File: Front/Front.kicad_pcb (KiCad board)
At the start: 2 copper layers, 40 x 40 mm, 42 parts, among them J1 USB_B_Micro, Q1 BC849, Q2 BC849, SW2 SW_Push, U1 CH340C, U10 ESP32-WROOM-32, U2 CJVL53L0XV2, U3 SPX3819M5-L-3-3

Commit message: V0.2: Redo front schematic and PCB
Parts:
- removed D1: BLUE, LED_SMD:LED_0805_2012Metric_Pad1.15x1.40mm_HandSolder
- removed D2: GREEN, LED_SMD:LED_0805_2012Metric_Pad1.15x1.40mm_HandSolder
- removed G***: LOGO, Print:d1
- removed H17: VBS, Custom:Mounting_Pad_Power
- removed SW2: SW_Push, Button_Switch_SMD:Panasonic_EVQPUJ_EVQPUA
- added H25: LED1, Custom:Mounting_Pad_Signal, F.Cu at (205.7, 105.0)
- added H26: LED2, Custom:Mounting_Pad_Signal, F.Cu at (208.3, 105.0)
- added H27: TCH2, Custom:Mounting_Pad_Touch, F.Cu at (210.8, 104.2)
- added H28: TCH1, Custom:Mounting_Pad_Touch, F.Cu at (220.2, 104.2)
- added SW1: SW_DPDT_x2, Custom:JS102011SAQN, F.Cu at (230.7, 112.7)
- H1: value VBUS -> PWR
- H16: value ORST -> O~RST
- R3, R4: value 150 -> 510
- moved R18 27.6 mm to (204.4, 122.8)
- moved U3 27.5 mm to (227.2, 112.7), turned to 90 degrees
- moved R4 26.8 mm to (204.4, 129.9), turned to 90 degrees
- moved R3 24.7 mm to (204.4, 126.3), turned to 90 degrees
- moved Q1 6.78 mm to (197.3, 133.7), turned to 180 degrees
- moved Q2 6.68 mm to (203.9, 133.7), turned to 0 degrees
- moved R2 3.85 mm to (200.7, 132.2), turned to 180 degrees
- moved H1 3.50 mm to (200.2, 105.5)
- moved H11 3.50 mm to (203.2, 105.0)
- moved U1 3.11 mm to (199.4, 124.5)
- moved C1 2.28 mm to (199.4, 118.3), turned to 0 degrees
- moved R1 1.15 mm to (200.7, 135.2), turned to 180 degrees
- moved C2 0.97 mm to (204.4, 119.2)
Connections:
- R3 pad 1: Net-(D1-Pad2) -> /TOUCH1
- R3 pad 2: /STATUS_LED_BLUE -> Net-(H28-Pad1)
- R4 pad 2: /STATUS_LED_GRN -> /TOUCH2
- U10 pad 10: (no net) -> /LED1
- U10 pad 11: (no net) -> /LED2
- U10 pad 12: /ED_IN1 -> /M1_AOUT2
- U10 pad 13: (no net) -> /M1_BOUT1
- U10 pad 14: (no net) -> /M1_BOUT2
- U10 pad 16: /M1_BOUT2 -> /M1_AOUT1
- U10 pad 17: /M1_BOUT1 -> (no net)
- U10 pad 18: /M1_AOUT2 -> (no net)
- U10 pad 19: /M1_AOUT1 -> (no net)
- U10 pad 20: /M2_AOUT1 -> (no net)
- U10 pad 21: /M2_AOUT2 -> (no net)
- U10 pad 22: /M2_BOUT1 -> (no net)
- U10 pad 23: /M2_BOUT2 -> /M2_AOUT1
- U10 pad 24: /M1_M2_~SLEEP -> /M2_AOUT2
- U10 pad 26: (no net) -> /M2_BOUT1
- U10 pad 27: /ED_IN2 -> /M2_BOUT2
- U10 pad 28: /OD_SCL -> /M1_M2_~SLEEP
- U10 pad 29: /OD_SDA -> /OD_SCL
- U10 pad 30: /OD_SHUT -> /OD_SDA
- U10 pad 31: /OD_INTERRUPT -> /OD_SHUT
- U10 pad 4: (no net) -> /ED_IN1
- U10 pad 5: (no net) -> /ED_IN2
- U10 pad 7: /STATUS_LED_GRN -> /OD_INTERRUPT
- U10 pad 8: /STATUS_LED_BLUE -> /TOUCH1
- U10 pad 9: (no net) -> /TOUCH2
- U3 pad 1: VBUS -> Net-(SW1-Pad2)
- U3 pad 3: VBUS -> Net-(SW1-Pad2)
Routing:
- net Net-(H28-Pad1): track 0.00 -> 43.8 mm, vias 0 -> 2
- net Net-(H27-Pad1): track 2.14 -> 38.5 mm, vias 0 -> 2
- net /STATUS_LED_BLUE: track 35.8 -> 0.00 mm
- net /LED2: track 0.00 -> 33.2 mm
- net /STATUS_LED_GRN: track 32.2 -> 0.00 mm
- net /LED1: track 0.00 -> 31.1 mm
- net /~RST: track 52.8 -> 27.0 mm
- net VBUS: track 21.9 -> 44.7 mm, vias 5 -> 2
- net /ED_IN2: track 11.1 -> 32.6 mm, vias 0 -> 4
- net +3V3: track 96.7 -> 111.3 mm, vias 8 -> 6
- net /ED_IN1: track 15.2 -> 26.5 mm, vias 0 -> 2
- net /GPIO0: track 30.0 -> 21.6 mm
- net /OD_INTERRUPT: track 17.7 -> 25.8 mm, vias 0 -> 2
- net Net-(SW1-Pad2): track 0.00 -> 7.93 mm
- net GND: track 27.1 -> 20.2 mm, vias 43 -> 36
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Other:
- outline, holes or cut-outs redrawn
- board text added: "Cuby V0.2"
- board text removed: "Cuby V0.1"

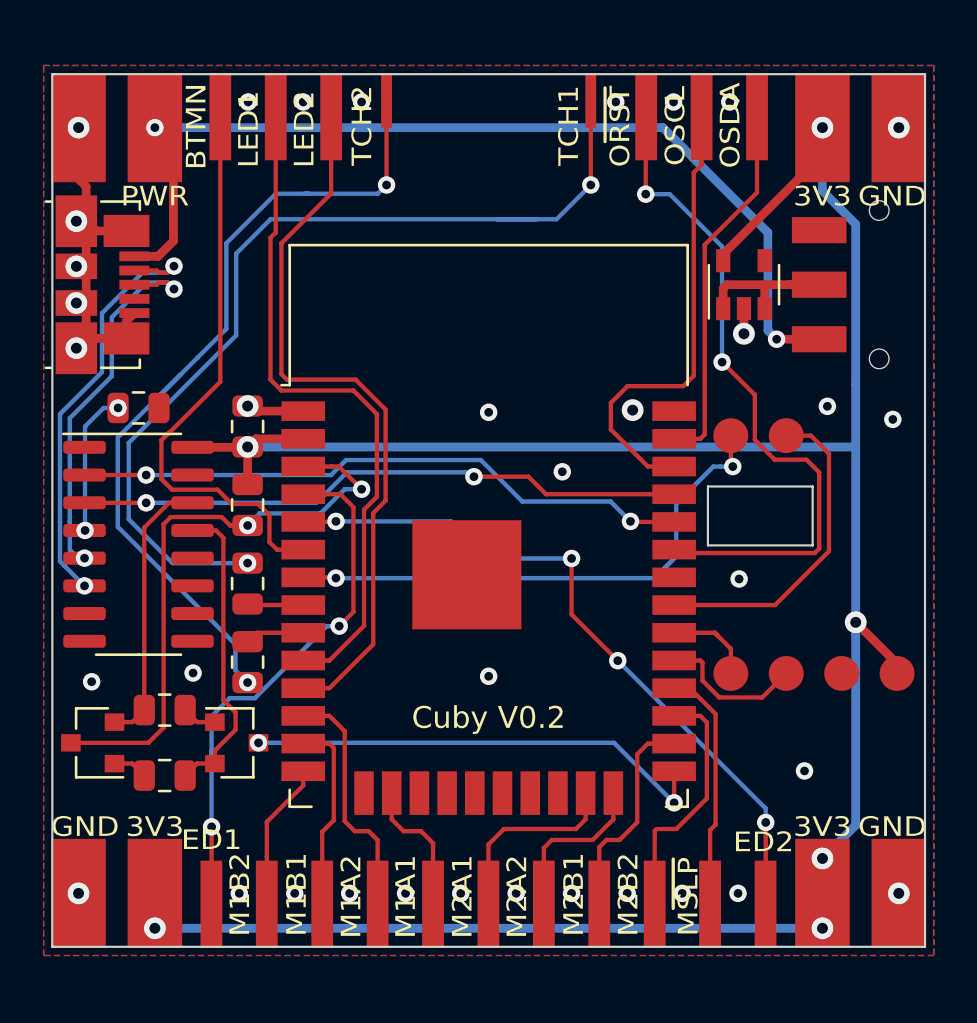
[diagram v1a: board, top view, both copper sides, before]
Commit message: updated bottom (motor placement, sharp sensor), front redesign, start op top redesign
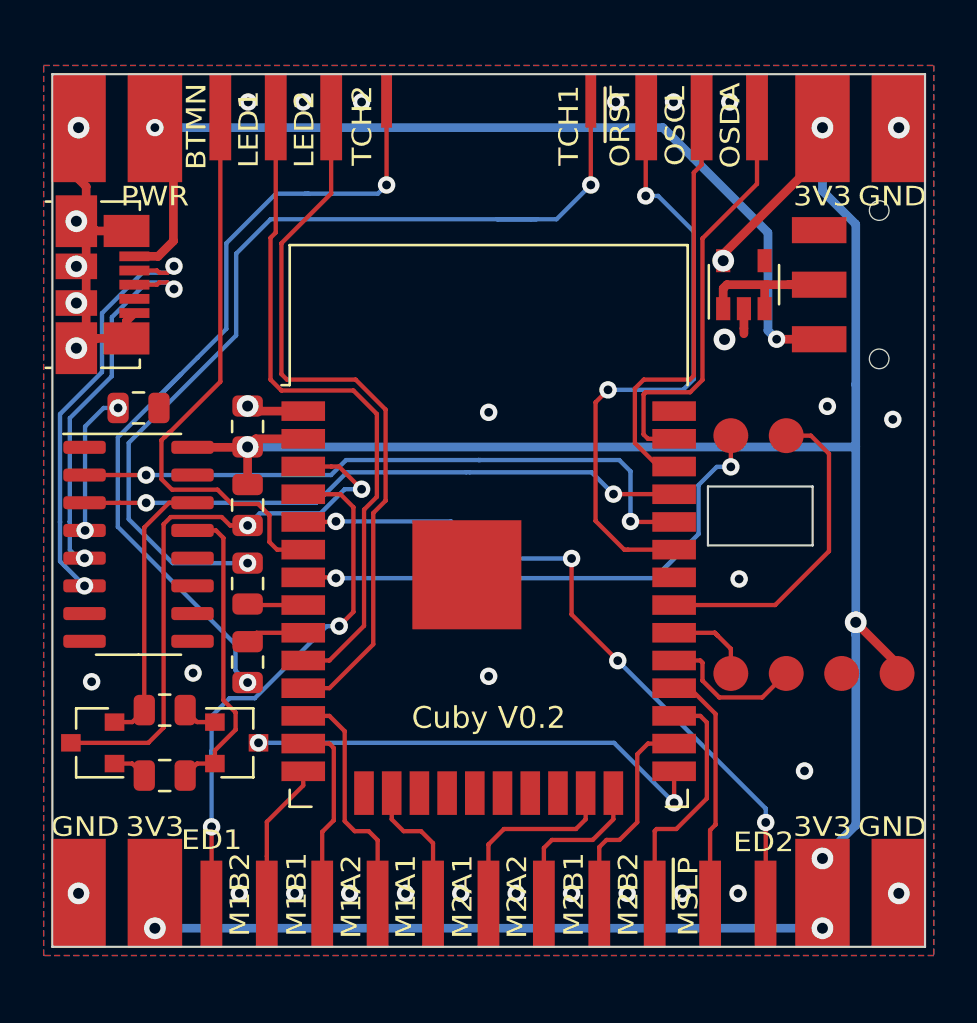
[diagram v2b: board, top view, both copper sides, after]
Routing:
- net /OLED_~RES: track 31.4 -> 27.8 mm
- net /OLED_SDA: track 17.0 -> 19.4 mm
- net /TXD-RXD: track 28.5 -> 29.9 mm
- net /OLED_SCL: track 21.2 -> 19.7 mm
- net GND: vias 36 -> 34
- net +3V3: vias 6 -> 7

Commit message: Update Top V0.2, small changes to motor placement
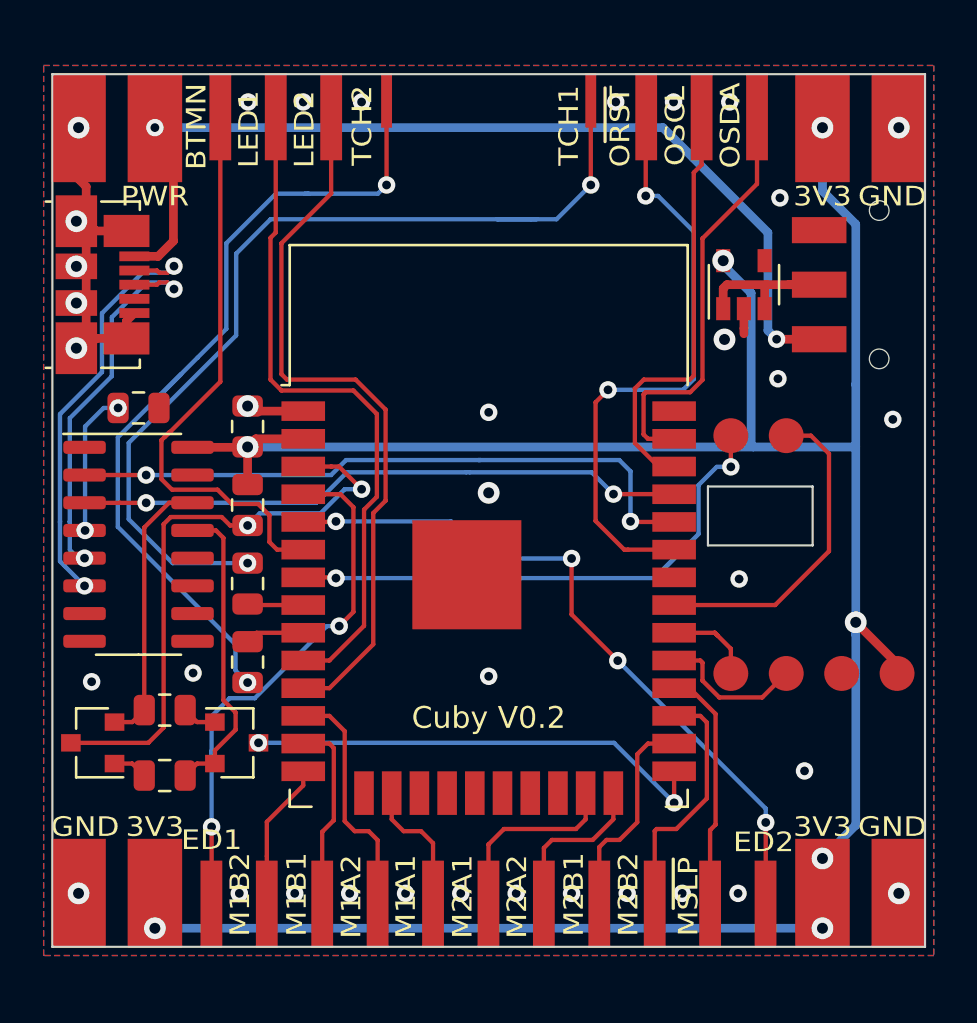
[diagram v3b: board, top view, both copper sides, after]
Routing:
- net +3V3: track 111.3 -> 113.7 mm
- net GND: vias 34 -> 36
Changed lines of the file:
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@@
     (thickness 1.6)
     (drawings 9)
-    (tracks 418)
+    (tracks 423)
     (zones 0)
     (modules 42)
@@
   (via (at 204.45 118.2125) (size 1) (drill 0.5) (layers F.Cu B.Cu) (net 1) (status 30))
   (via (at 234.025 118.825) (size 0.8) (drill 0.4) (layers F.Cu B.Cu) (net 1))
-  (via (at 231.025 118.225) (size 0.8) (drill 0.4) (layers F.Cu B.Cu) (net 1))
+  (via (at 228.76 116.96) (size 0.8) (drill 0.4) (layers F.Cu B.Cu) (net 1))
+  (via (at 228.85 108.67) (size 0.8) (drill 0.4) (layers F.Cu B.Cu) (net 1))
+  (via (at 215.5 122.19) (size 1) (drill 0.5) (layers F.Cu B.Cu) (net 1))
   (via (at 197.00001 123.915) (size 0.8) (drill 0.4) (layers F.Cu B.Cu) (net 2) (status 30))
   (via (at 198.5125 118.3) (size 0.8) (drill 0.4) (layers F.Cu B.Cu) (net 2) (status 30))
@@
   (segment (start 230.8 108.35) (end 232.325 109.875) (width 0.4) (layer B.Cu) (net 4))
   (segment (start 230.8 105.45) (end 230.8 108.35) (width 0.4) (layer B.Cu) (net 4))
-  (segment (start 226.25 111.25) (end 226.25 111.55) (width 0.4) (layer F.Cu) (net 4) (status 30))
-  (segment (start 230.8 106.7) (end 226.25 111.25) (width 0.4) (layer F.Cu) (net 4) (status 30))
   (segment (start 230.8 105.45) (end 230.8 106.7) (width 0.4) (layer F.Cu) (net 4) (status 30))
   (via (at 204.45 120.0875) (size 1) (drill 0.5) (layers F.Cu B.Cu) (net 4) (status 30))
@@
   (segment (start 232.325 120.075) (end 232.325 128.125) (width 0.4) (layer B.Cu) (net 4))
   (segment (start 232.3125 120.0875) (end 232.325 120.075) (width 0.4) (layer B.Cu) (net 4))
-  (segment (start 204.45 120.0875) (end 232.3125 120.0875) (width 0.4) (layer B.Cu) (net 4))
   (via (at 226.25 111.55) (size 1) (drill 0.5) (layers F.Cu B.Cu) (net 4))
+  (segment (start 226.25 111.755) (end 227.53 113.035) (width 0.4) (layer B.Cu) (net 4))
+  (segment (start 226.25 111.55) (end 226.25 111.755) (width 0.4) (layer B.Cu) (net 4))
+  (segment (start 227.53 119.99) (end 227.6275 120.0875) (width 0.4) (layer B.Cu) (net 4))
+  (segment (start 227.53 113.035) (end 227.53 119.99) (width 0.4) (layer B.Cu) (net 4))
+  (segment (start 204.45 120.0875) (end 227.6275 120.0875) (width 0.4) (layer B.Cu) (net 4))
+  (segment (start 227.6275 120.0875) (end 232.3125 120.0875) (width 0.4) (layer B.Cu) (net 4))
   (segment (start 203.65 123.6875) (end 203.2625 123.3) (width 0.2) (layer F.Cu) (net 5))
   (segment (start 204.45 123.6875) (end 203.65 123.6875) (width 0.2) (layer F.Cu) (net 5) (status 10))

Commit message: finish top, changes to front, added graphic
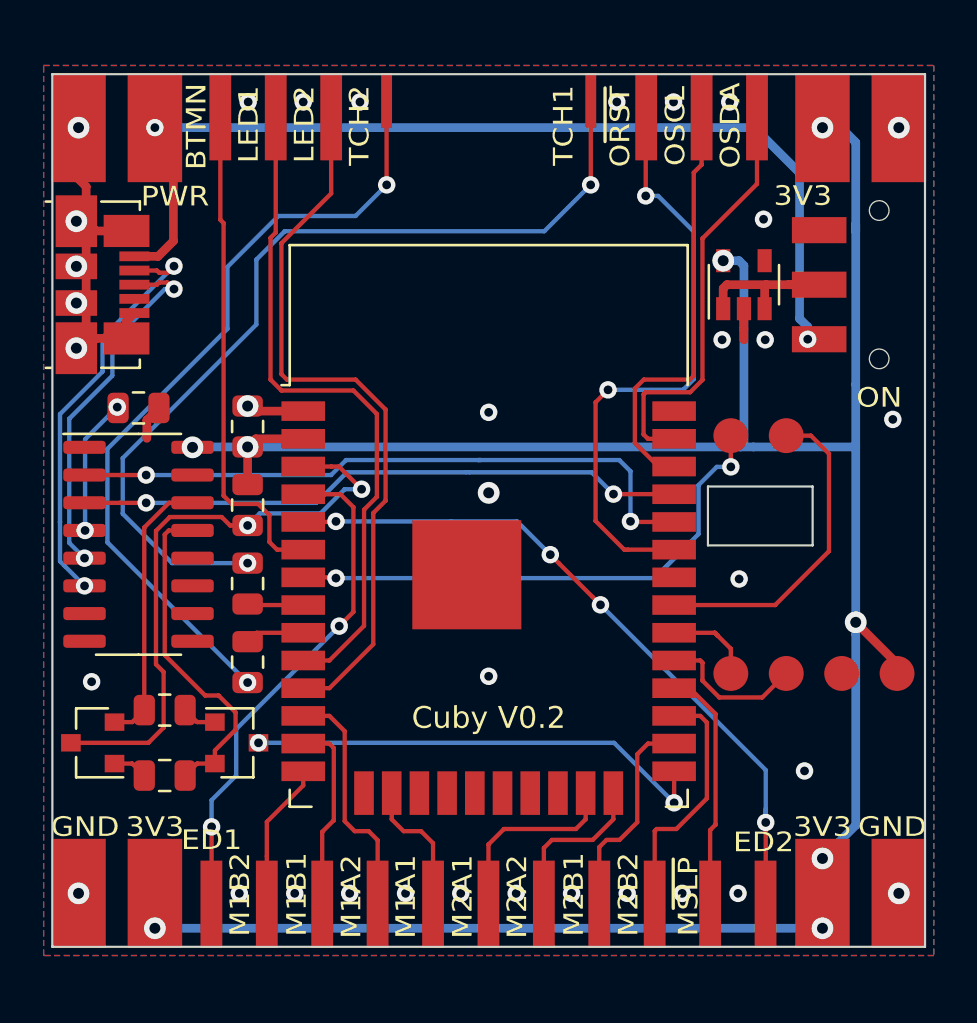
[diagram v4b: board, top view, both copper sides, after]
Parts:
- added G1: Graphic, Print:d1, B.Cu at (215.5, 123.0)
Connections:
- net Net-(H27-Pad1) renamed /T2
- net Net-(H28-Pad1) renamed /T1
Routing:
- net /BAT_MON: track 26.6 -> 22.8 mm
- net /T1: track 43.8 -> 41.5 mm
- net GND: track 20.2 -> 22.1 mm, vias 36 -> 35
- net /T2: track 38.5 -> 36.8 mm
- net /ED_IN1: track 26.5 -> 24.9 mm
- net Net-(Q2-Pad2): track 14.1 -> 15.5 mm
- net +3V3: track 113.7 -> 114.8 mm, vias 7 -> 8
- net VBUS: track 44.7 -> 45.8 mm
- net /D+: track 18.0 -> 17.1 mm
- net /D-: track 20.0 -> 19.3 mm
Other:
- net class Touch added: clearance 0.5, trace_width 0.2, via_dia 0.8, via_drill 0.4
- board text added: "ON"

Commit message: finishing touches, moved touch traces to back
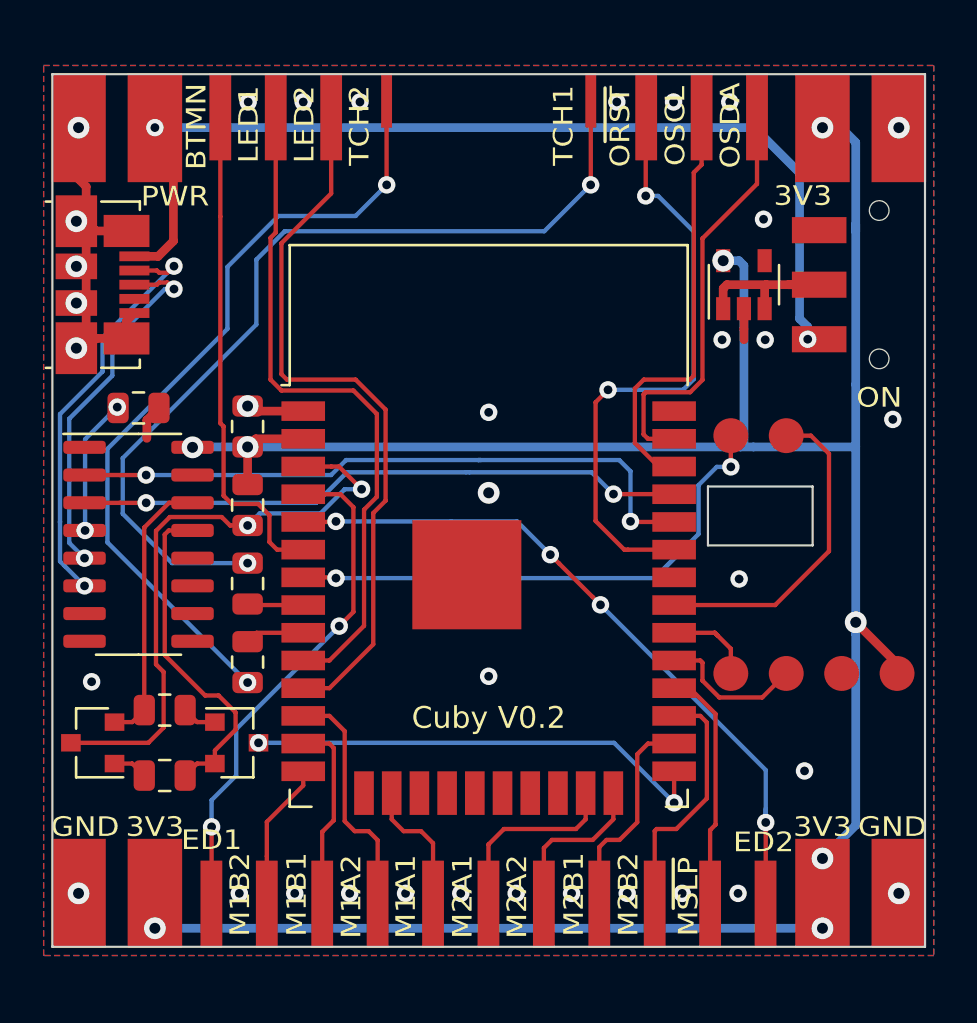
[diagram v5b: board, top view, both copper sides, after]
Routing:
- net +3V3: track 114.8 -> 113.6 mm
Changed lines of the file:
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@@
   (segment (start 204.4325 120.105) (end 204.45 120.0875) (width 0.4) (layer F.Cu) (net 4) (status 30))
   (segment (start 204.45 121.8125) (end 204.45 120.0875) (width 0.4) (layer F.Cu) (net 4) (status 30))
-  (segment (start 230.8 105.45) (end 230.8 106.7) (width 0.4) (layer F.Cu) (net 4) (status 30))
   (via (at 204.45 120.0875) (size 1) (drill 0.5) (layers F.Cu B.Cu) (net 4) (status 30))
   (segment (start 232.325 137.425) (end 230.8 138.95) (width 0.4) (layer B.Cu) (net 4))
@@
   (segment (start 207 135.605) (end 205.33 137.275) (width 0.2) (layer F.Cu) (net 14))
   (segment (start 207 134.955) (end 207 135.605) (width 0.2) (layer F.Cu) (net 14) (status 10))
+  (segment (start 203.2 109.525) (end 203.2 104.95) (width 0.2) (layer F.Cu) (net 15))
+  (segment (start 203.2 119) (end 203.2 109.525) (width 0.2) (layer F.Cu) (net 15))
+  (segment (start 203.34999 122.322906) (end 203.34999 119.14999) (width 0.2) (layer F.Cu) (net 15))
+  (segment (start 207 124.795) (end 205.8 124.795) (width 0.2) (layer F.Cu) (net 15))
   (segment (start 205.8 124.795) (end 205.45001 124.44501) (width 0.2) (layer F.Cu) (net 15))
-  (segment (start 207 124.795) (end 205.8 124.795) (width 0.2) (layer F.Cu) (net 15) (status 10))
   (segment (start 205.45001 124.44501) (end 205.45001 123.218516) (width 0.2) (layer F.Cu) (net 15))
   (segment (start 205.45001 123.218516) (end 204.931504 122.70001) (width 0.2) (layer F.Cu) (net 15))
   (segment (start 204.931504 122.70001) (end 203.727094 122.70001) (width 0.2) (layer F.Cu) (net 15))
-  (segment (start 203.34999 109.82499) (end 203.2 109.675) (width 0.2) (layer F.Cu) (net 15))
-  (segment (start 203.34999 122.322906) (end 203.34999 109.82499) (width 0.2) (layer F.Cu) (net 15))
+  (segment (start 203.34999 119.14999) (end 203.2 119) (width 0.2) (layer F.Cu) (net 15))
   (segment (start 203.727094 122.70001) (end 203.34999 122.322906) (width 0.2) (layer F.Cu) (net 15))
-  (segment (start 203.2 104.95) (end 203.2 109.675) (width 0.2) (layer F.Cu) (net 15))
   (segment (start 202.79 139.55) (end 202.79 141.05) (width 0.2) (layer F.Cu) (net 16) (status 30))
   (via (at 208.65 128.3) (size 0.8) (drill 0.4) (layers F.Cu B.Cu) (net 16))
